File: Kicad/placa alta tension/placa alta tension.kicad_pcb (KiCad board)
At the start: 2 copper layers, 68.6 x 53.3 mm, 8 parts, among them J1 Power, J2 Digital/PWM, J3 Analog, J4 Digital/PWM

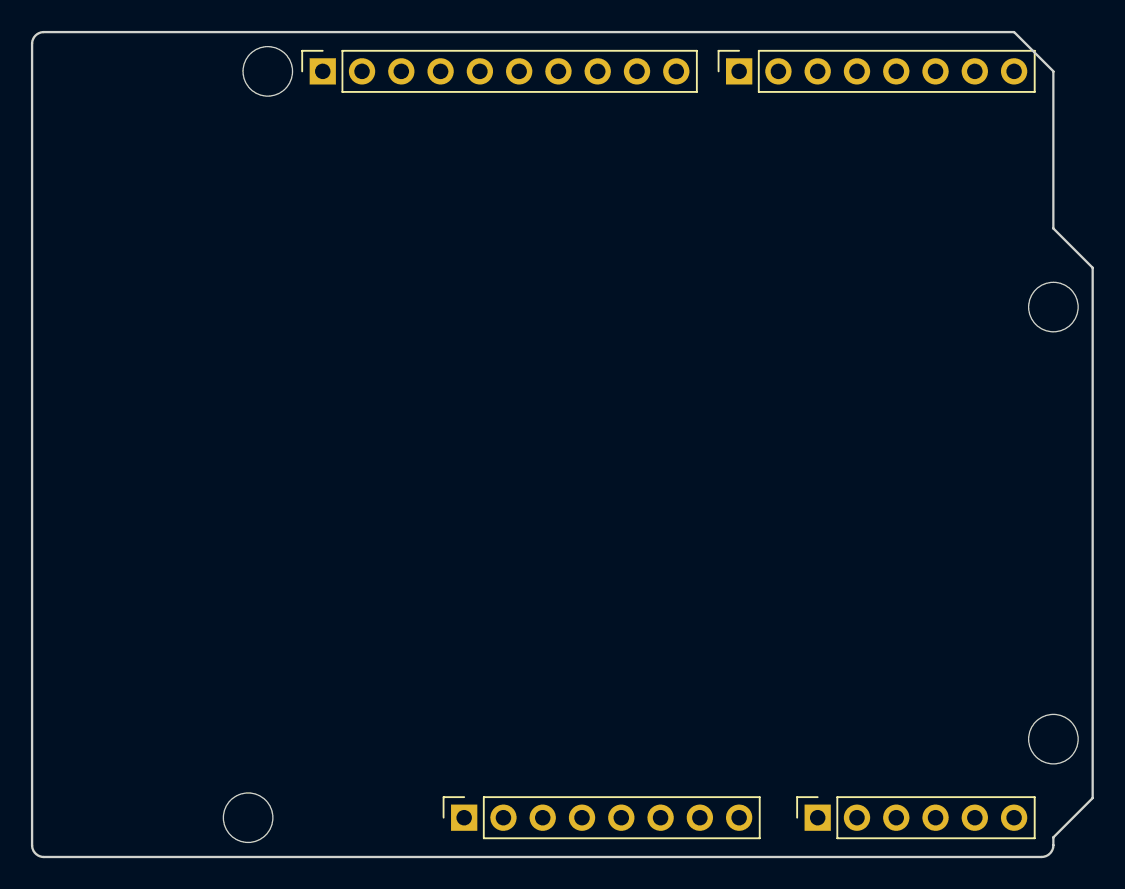
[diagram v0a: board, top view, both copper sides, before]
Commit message: shield arrancado
Faltaría rutear y ver si podemos hacer algo para fabricarlo nosotros o si o si va a tener que ser doble faz. Sería interesante probar fabricar en china.
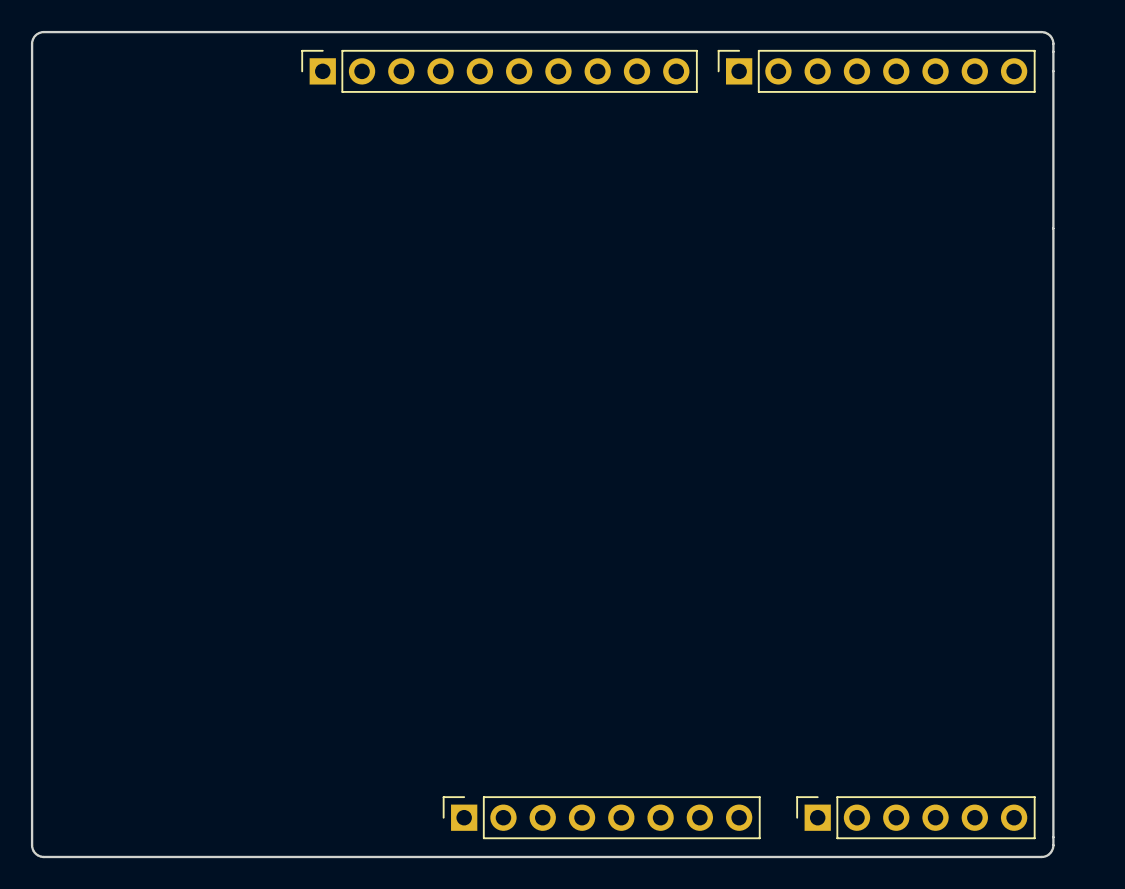
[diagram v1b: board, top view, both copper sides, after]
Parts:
- removed MH1, MH2, MH3, MH4: MountingHole_3.2mm, Arduino_MountingHole:MountingHole_3.2mm
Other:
- board size 68.6 x 53.3 mm -> 66 x 53.3 mm
- board text removed: "ICSP"
